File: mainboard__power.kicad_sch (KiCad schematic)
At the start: 33 parts

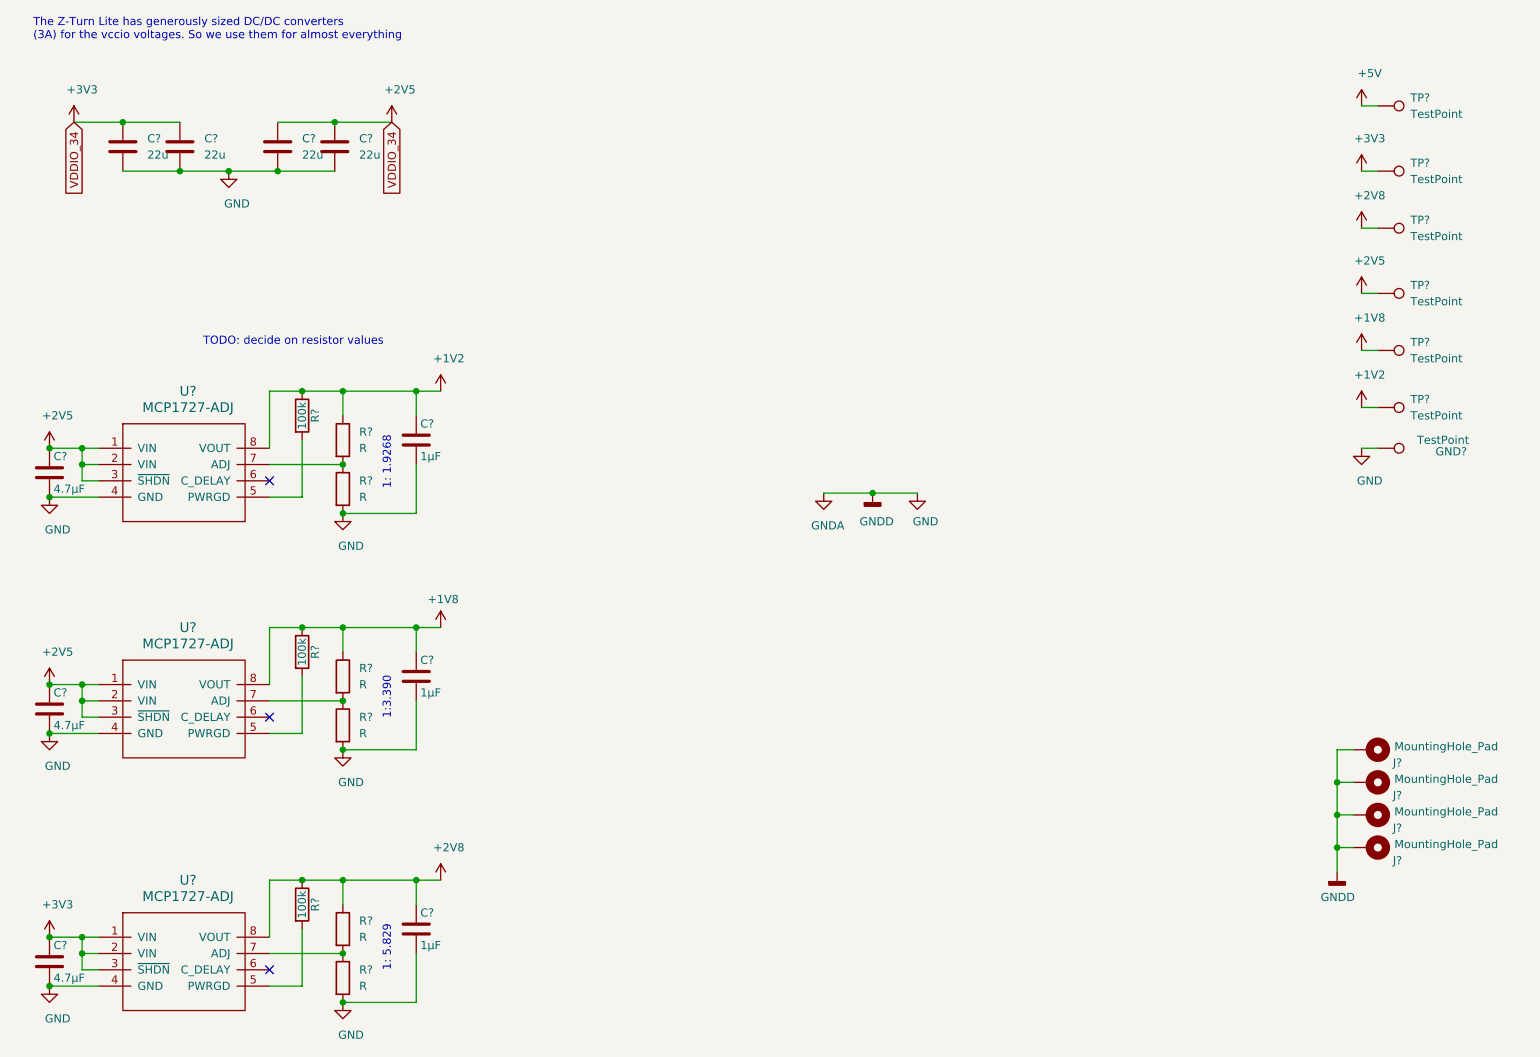
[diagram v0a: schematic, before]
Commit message: small tweaks; add mipi termination
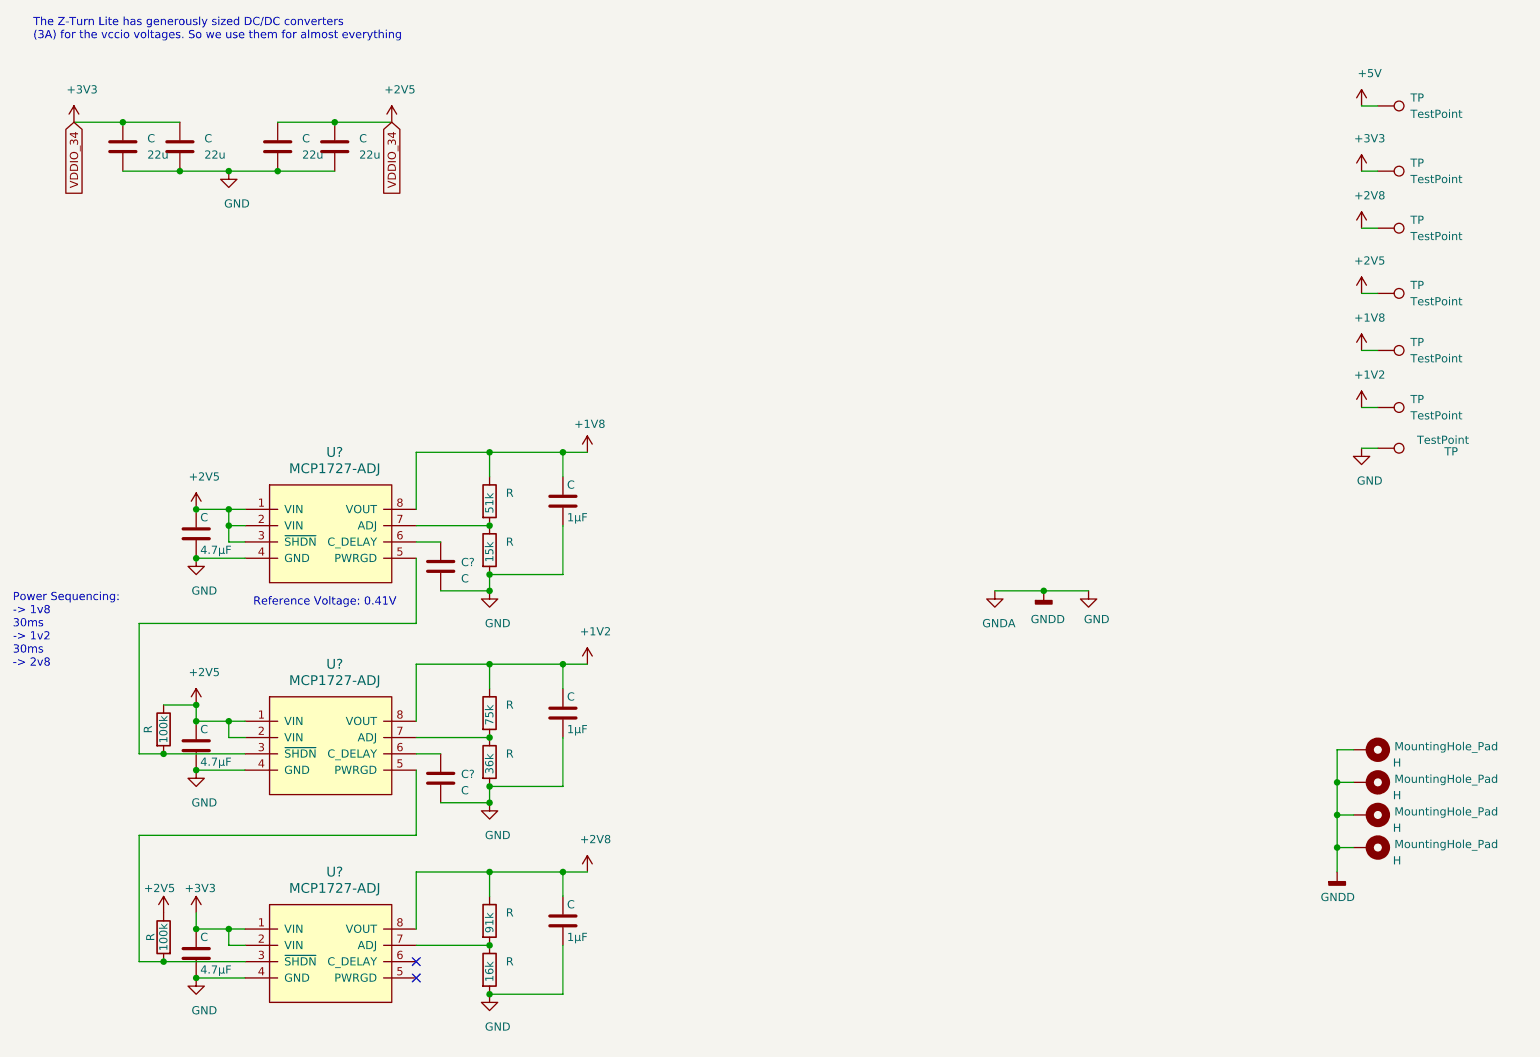
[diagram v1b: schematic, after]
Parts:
- removed R?: 100k, Resistors_SMD:R_0603_HandSoldering, symbol Device:R
- added C? (x2): C, symbol Device:C
- R: renamed from R?; value R -> 51k
- R: renamed from R?; value R -> 91k
- R: renamed from R?; value R -> 36k
- R: renamed from R?; value R -> 15k
- R: renamed from R?; value R -> 75k
- R: renamed from R?; value R -> 16k
- U? (x3): symbol parts:MCP1727-ADJ -> ic:MCP1727-ADJ
- gave numbers to parts that had none: 5
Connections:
- net +1V2: no longer R.1
- net +2V5: now also R.1, R.1; no longer U?.3 (~SHDN), U?.3 (~SHDN)
- net +2V8: no longer R.1
- net GND: now also C?.2, C?.2
- net at U?.5 (PWRGD): now also R.2, U?.3 (~SHDN)
- net at R.2: now also U?.3 (~SHDN), U?.5 (PWRGD); no longer U?.5 (PWRGD)
- net at U?.6 (C_DELAY): now also C?.1 (x2)
- no-connect marks 3 -> 2
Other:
- note added: "Power Sequencing: -> 1v8 30ms -> 1v2 30ms -> 2v8"
- note added: "Reference Voltage: 0.41V"
- note removed: "1: 1.9268"
- note removed: "1: 5.829"
- note removed: "1:3.390"
- note removed: "TODO: decide on resistor values"
- moved on the sheet: C, R
